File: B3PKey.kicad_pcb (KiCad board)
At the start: 2 copper layers, 177 parts, among them SW1 SW_Push, U1 ATmega32U4-AU, Y1 16MHz

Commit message: Add edge cuts and place some components
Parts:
- moved C1 126.0 mm to (213.6, 227.9)
- moved C2 126.0 mm to (218.0, 227.9)
- moved C7 126.0 mm to (226.8, 227.9)
- moved F1 126.0 mm to (222.2, 222.3)
- moved R4 126.0 mm to (213.6, 222.0)
- moved C4 126.0 mm to (222.3, 224.9)
- moved C6 126.0 mm to (213.5, 224.9)
- moved R1 126.0 mm to (209.2, 221.5)
- moved SW1 126.0 mm to (206.5, 226.2)
- moved Y1 126.0 mm to (204.4, 220.8)
- moved C5 126.0 mm to (217.9, 224.9)
- moved U1 105.5 mm to (193.7, 182.6)
- moved D15 94.3 mm to (92.1, 112.7)
- moved D17 94.3 mm to (130.2, 112.7)
- moved D19 94.3 mm to (168.3, 112.7)
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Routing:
- net D+: track 0.00 -> 5.11 mm
- net D-: track 0.00 -> 5.10 mm
- net Net-(R3-Pad1): track 0.00 -> 3.38 mm, vias 0 -> 2
- net Net-(R2-Pad1): track 0.00 -> 3.36 mm, vias 0 -> 2
- net ROW5: vias 0 -> 2
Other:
- board outline added: 265.7 x 115.3 mm

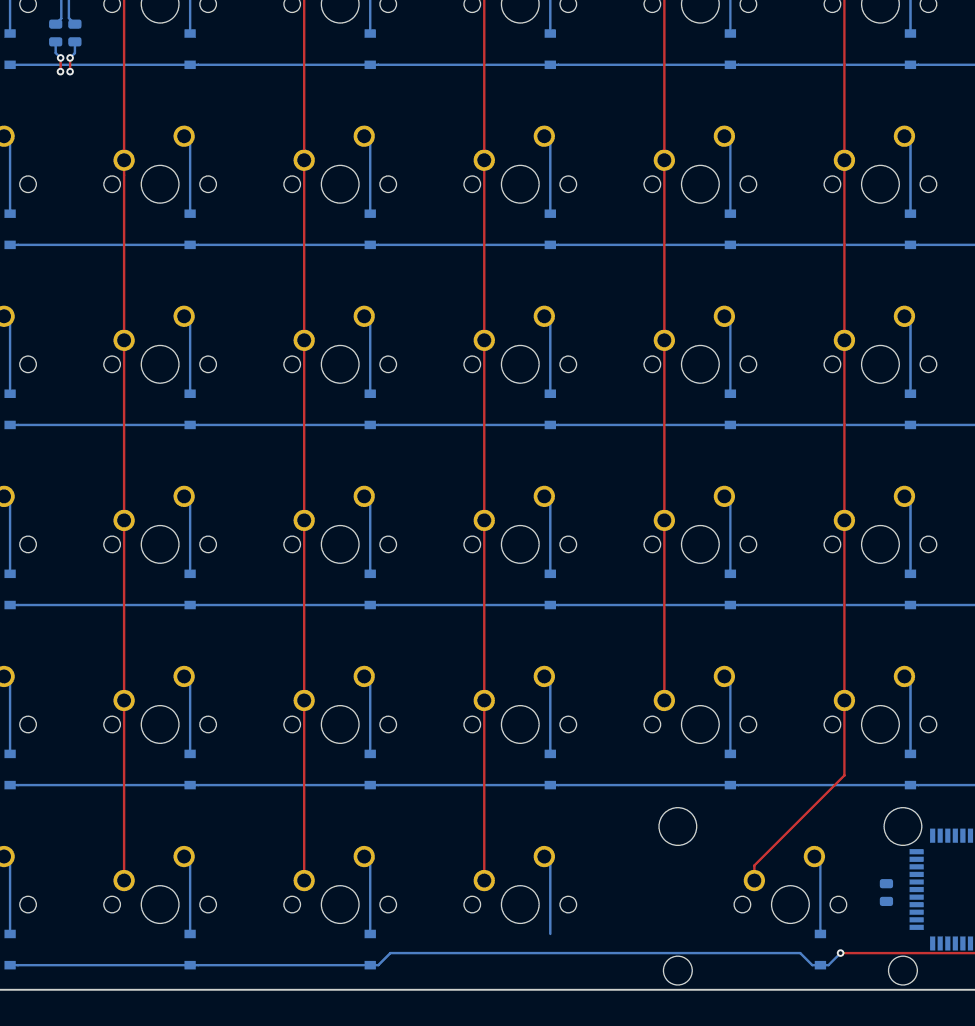
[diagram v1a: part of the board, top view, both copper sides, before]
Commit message: Route USB traces
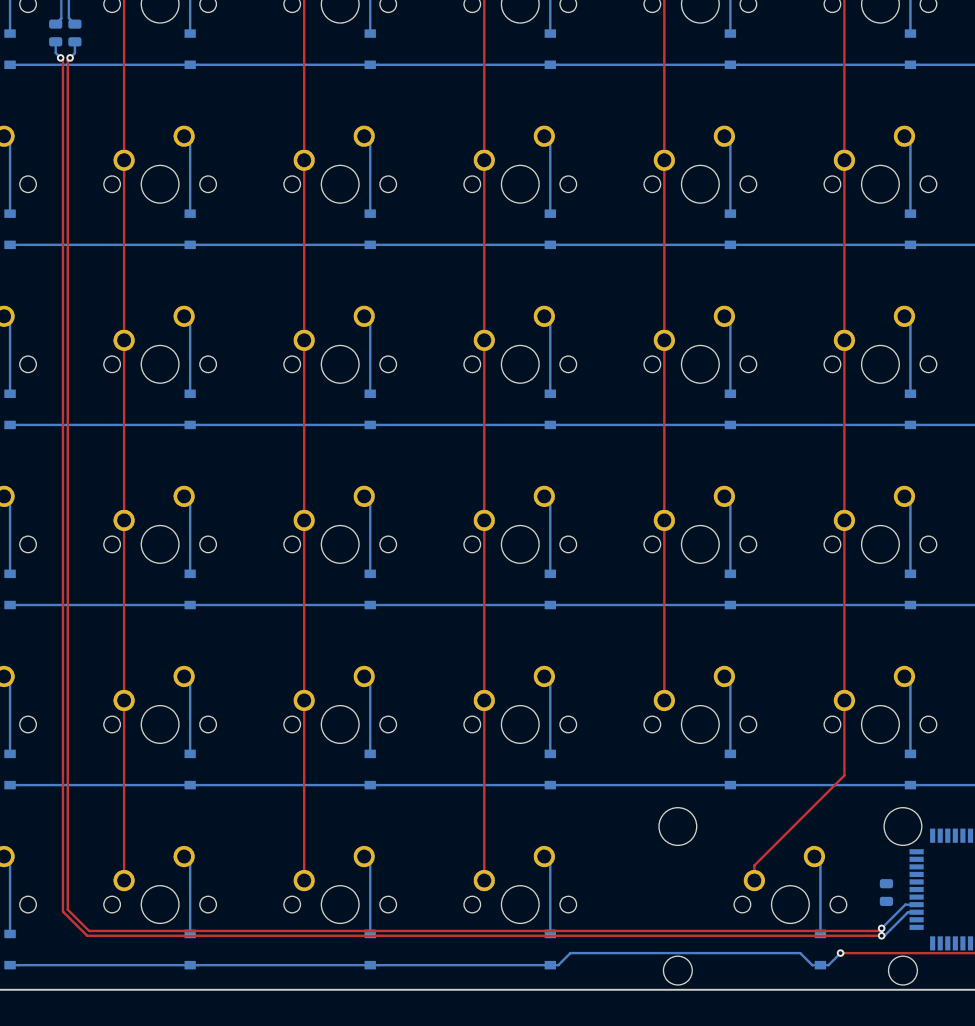
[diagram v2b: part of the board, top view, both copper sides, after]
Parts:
- added D73: D_Small, Diode_SMD:D_SOD-123, B.Cu at (149.2, 188.9)
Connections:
- net Net-(R2-Pad1) renamed /D_P
- net Net-(R3-Pad1) renamed /D_N
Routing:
- net /D_N: track 3.38 -> 184.8 mm
- net /D_P: track 3.36 -> 184.0 mm

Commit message: Some routing
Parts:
- moved F1 182.3 mm to (94.7, 92.0), turned to 90 degrees
- moved C7 58.2 mm to (183.0, 189.7), turned to 270 degrees
- moved C1 28.0 mm to (194.6, 207.3)
- moved C2 28.0 mm to (199.0, 207.3)
- moved R4 28.0 mm to (194.6, 201.4)
- moved C4 28.0 mm to (203.3, 204.3)
- moved R1 28.0 mm to (190.2, 200.9)
- moved SW1 28.0 mm to (187.5, 205.6)
- moved C5 28.0 mm to (198.9, 204.3)
- moved C6 28.0 mm to (194.5, 204.3)
- moved Y1 28.0 mm to (185.3, 200.2)
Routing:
- net +5V: track 0.00 -> 180.5 mm, vias 0 -> 2
- net VCC: track 0.00 -> 5.71 mm
- net ROW4: vias 0 -> 2

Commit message: Route more traces
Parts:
- moved SW1 31.9 mm to (179.7, 174.6), turned to 180 degrees
- moved C4 31.0 mm to (193.8, 174.9)
- moved R1 27.0 mm to (190.4, 174.0)
- moved C5 25.5 mm to (202.1, 179.1)
- moved R4 14.6 mm to (200.7, 188.1), turned to 180 degrees
- moved C6 14.0 mm to (198.1, 190.9), turned to 270 degrees
- moved C1 12.9 mm to (182.0, 204.2), turned to 270 degrees
- moved C2 11.1 mm to (188.3, 204.2), turned to 90 degrees
- moved Y1 4.02 mm to (185.2, 204.2)
- moved C3 0.52 mm to (185.3, 183.0), turned to 180 degrees
- moved U1 0.06 mm to (193.7, 182.5)
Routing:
- net +5V: track 180.5 -> 248.1 mm, vias 2 -> 7
- net Net-(R1-Pad2): track 0.00 -> 12.7 mm
- net /D_P: track 184.0 -> 180.3 mm
- net /D_N: track 184.8 -> 181.2 mm
- net Net-(C3-Pad1): track 0.00 -> 1.95 mm
- net Net-(R4-Pad2): track 0.00 -> 1.73 mm

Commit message: Move components to forehead and route all traces
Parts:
- moved C2 153.5 mm to (124.7, 64.6), turned to 225 degrees
- moved Y1 149.2 mm to (126.9, 66.8), turned to 135 degrees
- moved C1 145.1 mm to (129.2, 69.1), turned to 45 degrees
- moved C3 134.3 mm to (112.9, 69.8), turned to 135 degrees
- moved C7 133.8 mm to (105.5, 80.5), turned to 315 degrees
- moved C6 132.8 mm to (118.7, 84.5), turned to 315 degrees
- moved U1 130.4 mm to (118.9, 75.7), turned to 315 degrees
- moved R4 129.3 mm to (120.1, 86.9), turned to 45 degrees
- moved R1 129.2 mm to (118.6, 66.5), turned to 135 degrees
- moved C4 128.8 mm to (122.0, 67.9), turned to 135 degrees
- moved SW1 128.4 mm to (108.0, 68.2), turned to 225 degrees
- moved C5 127.3 mm to (127.8, 75.7), turned to 45 degrees
- moved F1 16.1 mm to (94.9, 75.9)
- moved R2 16.1 mm to (99.1, 75.8)
- moved R3 16.1 mm to (97.0, 75.8)
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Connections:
- U1 pad 1: Net-(U1-Pad1) -> COL0
- U1 pad 10: Net-(U1-Pad10) -> COL2
- U1 pad 11: Net-(U1-Pad11) -> COL1
- U1 pad 20: Net-(U1-Pad20) -> COL13
- U1 pad 21: Net-(U1-Pad21) -> COL12
- U1 pad 22: Net-(U1-Pad22) -> COL11
- U1 pad 25: Net-(U1-Pad25) -> COL10
- U1 pad 26: Net-(U1-Pad26) -> COL9
- U1 pad 27: Net-(U1-Pad27) -> COL8
- U1 pad 28: Net-(U1-Pad28) -> COL7
- U1 pad 29: Net-(U1-Pad29) -> COL6
- U1 pad 30: Net-(U1-Pad30) -> COL5
- U1 pad 31: Net-(U1-Pad31) -> COL4
- U1 pad 32: Net-(U1-Pad32) -> COL3
- U1 pad 36: Net-(U1-Pad36) -> ROW5
- U1 pad 37: Net-(U1-Pad37) -> ROW4
- U1 pad 38: Net-(U1-Pad38) -> ROW3
- U1 pad 39: Net-(U1-Pad39) -> ROW2
- U1 pad 40: Net-(U1-Pad40) -> ROW1
- U1 pad 41: Net-(U1-Pad41) -> ROW0
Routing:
- net COL13: track 96.3 -> 310.8 mm, vias 0 -> 1
- net COL12: track 105.3 -> 299.7 mm, vias 0 -> 1
- net COL11: track 95.3 -> 269.6 mm, vias 0 -> 1
- net /D_P: track 180.3 -> 20.0 mm, vias 2 -> 0
- net /D_N: track 181.2 -> 21.0 mm, vias 2 -> 0
- net COL10: track 95.3 -> 253.3 mm, vias 0 -> 1
- net +5V: track 248.1 -> 92.9 mm, vias 7 -> 8
- net COL9: track 95.3 -> 234.1 mm, vias 0 -> 1
- net COL8: track 95.3 -> 214.9 mm, vias 0 -> 1
- net ROW5: track 250.9 -> 363.5 mm
- net COL7: track 76.2 -> 176.7 mm, vias 0 -> 1
- net ROW4: track 247.7 -> 341.5 mm, vias 2 -> 4
- net COL6: track 99.2 -> 180.5 mm, vias 0 -> 1
- net ROW3: track 239.0 -> 314.1 mm, vias 0 -> 2
- net COL5: track 99.2 -> 161.3 mm, vias 0 -> 1
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- added copper zone on B.Cu, net GND
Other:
- board outline removed
